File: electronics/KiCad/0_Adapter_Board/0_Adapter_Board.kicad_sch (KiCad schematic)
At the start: 15 parts, among them J1 Conn_01x10, J2 Conn_01x10, J3 Conn_01x04, J4 Conn_01x04, J5 Conn_01x03

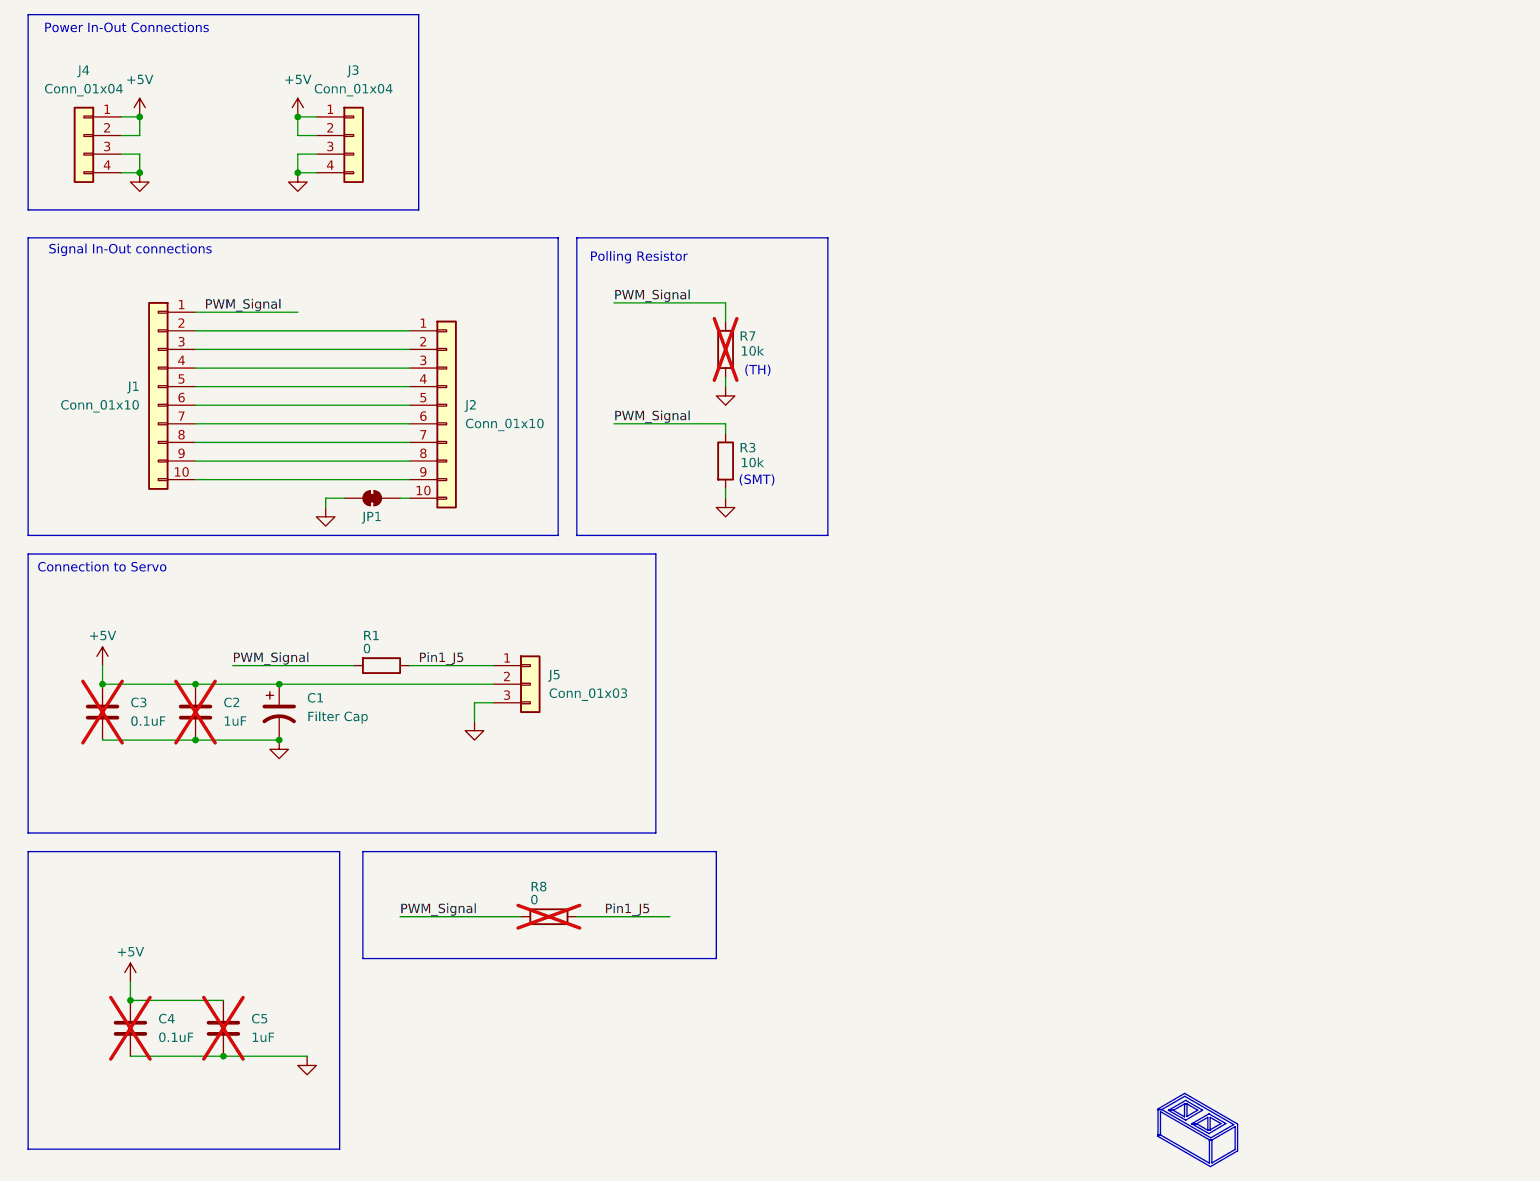
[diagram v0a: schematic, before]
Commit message: Updated to reflect V1.0 of layer board as well
Updated for initial orders with PCA module populated. Also updated to layer boards for flex cables.
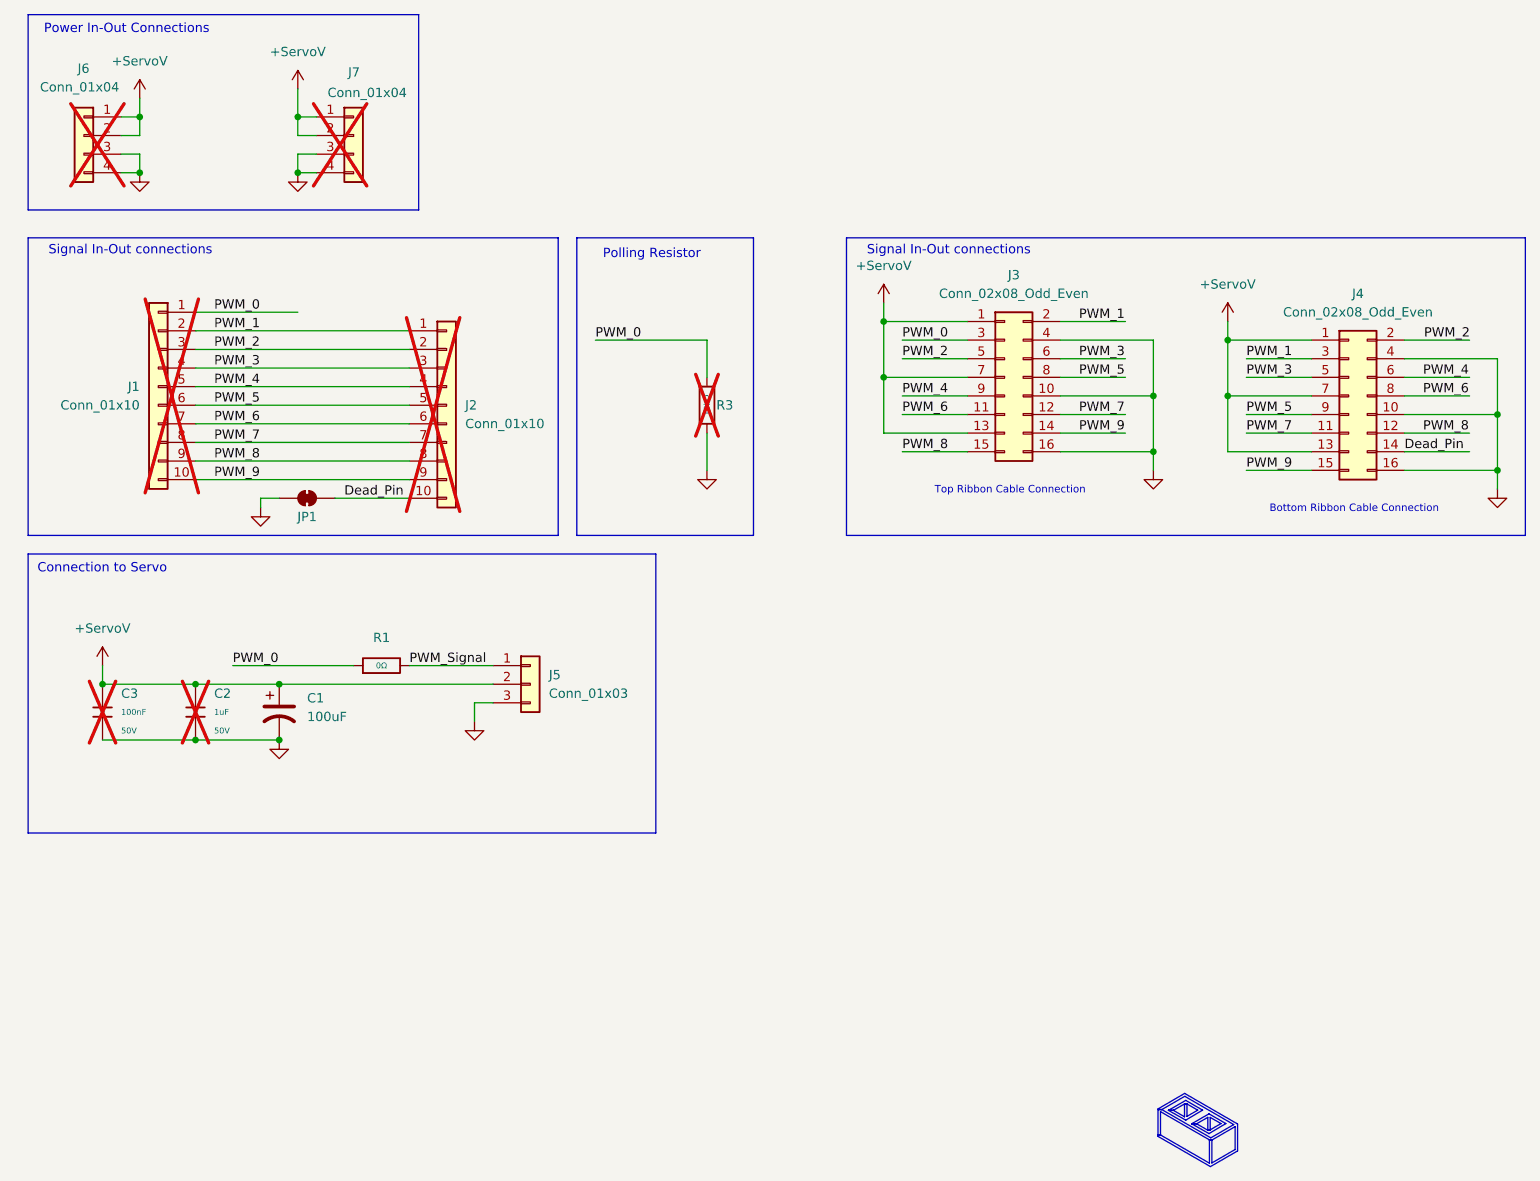
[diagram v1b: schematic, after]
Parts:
- removed C2: 1uF, Capacitor_SMD:C_0805_2012Metric_Pad1.18x1.45mm_HandSolder, symbol Device:C
- removed C3: 0.1uF, Capacitor_SMD:C_0805_2012Metric_Pad1.18x1.45mm_HandSolder, symbol Device:C
- removed C4: 0.1uF, Capacitor_THT:C_Disc_D7.5mm_W2.5mm_P5.00mm, symbol Device:C
- removed C5: 1uF, Capacitor_THT:C_Disc_D7.5mm_W2.5mm_P5.00mm, symbol Device:C
- removed J3, J4: Conn_01x04, Connector_JST:JST_XA_B04B-XASK-1-A_1x04_P2.50mm_Vertical, symbol Connector_Generic:Conn_01x04
- removed R1: 0, Resistor_SMD:R_0805_2012Metric_Pad1.20x1.40mm_HandSolder, symbol Device:R
- removed R3: 10k, Resistor_SMD:R_0805_2012Metric_Pad1.20x1.40mm_HandSolder, symbol Device:R
- removed R7: 10k, Resistor_THT:R_Axial_DIN0207_L6.3mm_D2.5mm_P10.16mm_Horizontal, symbol Device:R
- removed R8: 0, Resistor_THT:R_Axial_DIN0207_L6.3mm_D2.5mm_P10.16mm_Horizontal, symbol Device:R
- added C2: 1uF, PCM_JLCPCB:C_0603, symbol PCM_JLCPCB-Capacitors:0603,1uF
- added C3: 100nF, PCM_JLCPCB:C_0603, symbol PCM_JLCPCB-Capacitors:0603,100nF
- added J3, J4: Conn_02x08_Odd_Even, Connector_IDC:IDC-Header_2x08_P2.54mm_Vertical, symbol Connector_Generic:Conn_02x08_Odd_Even
- added J6, J7: Conn_01x04, Connector_JST:JST_XA_B04B-XASK-1-A_1x04_P2.50mm_Vertical, symbol Connector_Generic:Conn_01x04
- added R1: 0Ω, PCM_JLCPCB:R_0603, symbol PCM_JLCPCB-Resistors:0603,0Ω
- added R3: 10kΩ, PCM_JLCPCB:R_0603, symbol PCM_JLCPCB-Resistors:0603,10kΩ
- C1: value Filter Cap -> 100uF; footprint Capacitor_THT:CP_Radial_D8.0mm_P2.50mm -> EasyEDA:CAP-SMD_BD6.3-L6.6-W6.6-LS7.4-FD; LCSC (none) -> C2836442
- J1, J2: LCSC (none) -> C378928; now not fitted
- J5: LCSC (none) -> C492411
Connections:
- net Pin1_J5 is gone; now on net PWM_Signal: J5.1 (Pin_1)
- net GND: now also C2.2, C3.2, J3.10 (Pin_10), J3.16 (Pin_16), J3.4 (Pin_4), J4.10 (Pin_10), J4.16 (Pin_16), J4.4 (Pin_4), J6.3 (Pin_3), J6.4 (Pin_4), J7.3 (Pin_3), J7.4 (Pin_4), R3.2
- net PWM_Signal: now also R1.2; no longer J1.1 (Pin_1)
- net PWM_1: now reaches J1.2 (Pin_2), J2.1 (Pin_1)
- net PWM_1: now also J3.2 (Pin_2), J4.3 (Pin_3)
- net Dead_Pin: now reaches J2.10 (Pin_10), JP1.1 (A)
- net Dead_Pin: now also J4.14 (Pin_14)
- net PWM_2: now reaches J1.3 (Pin_3), J2.2 (Pin_2)
- net PWM_2: now also J3.5 (Pin_5), J4.2 (Pin_2)
- net PWM_3: now reaches J1.4 (Pin_4), J2.3 (Pin_3)
- net PWM_3: now also J3.6 (Pin_6), J4.5 (Pin_5)
- net PWM_4: now reaches J1.5 (Pin_5), J2.4 (Pin_4)
- net PWM_4: now also J3.9 (Pin_9), J4.6 (Pin_6)
- net PWM_5: now reaches J1.6 (Pin_6), J2.5 (Pin_5)
- net PWM_5: now also J3.8 (Pin_8), J4.9 (Pin_9)
- net PWM_6: now reaches J1.7 (Pin_7), J2.6 (Pin_6)
- net PWM_6: now also J3.11 (Pin_11), J4.8 (Pin_8)
- net PWM_7: now reaches J1.8 (Pin_8), J2.7 (Pin_7)
- net PWM_7: now also J3.12 (Pin_12), J4.11 (Pin_11)
- net PWM_8: now reaches J1.9 (Pin_9), J2.8 (Pin_8)
- net PWM_8: now also J3.15 (Pin_15), J4.12 (Pin_12)
- net PWM_9: now reaches J1.10 (Pin_10), J2.9 (Pin_9)
- net PWM_9: now also J3.14 (Pin_14), J4.15 (Pin_15)
- net +5V renamed +ServoV
- net +ServoV: now also C2.1, C3.1, J3.1 (Pin_1), J3.13 (Pin_13), J3.7 (Pin_7), J4.1 (Pin_1), J4.13 (Pin_13), J4.7 (Pin_7), J6.1 (Pin_1), J6.2 (Pin_2), J7.1 (Pin_1), J7.2 (Pin_2)
- new net PWM_0: J1.1 (Pin_1), J3.3 (Pin_3), R1.1, R3.1
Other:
- note added: "Bottom Ribbon Cable Connection"
- note added: "Top Ribbon Cable Connection"
- note removed: "(SMT)"
- note removed: "(TH)"
- moved on the sheet: JP1
